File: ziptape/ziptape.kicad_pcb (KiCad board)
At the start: 2 copper layers, 62.5 x 34 mm, 13 parts, among them J1 Cassette_Playback, J2 Cassette_Record, J3 Conn_RIOT, J4 Conn_Adapter_A, J5 Conn_Adapter_B, U1 LM339

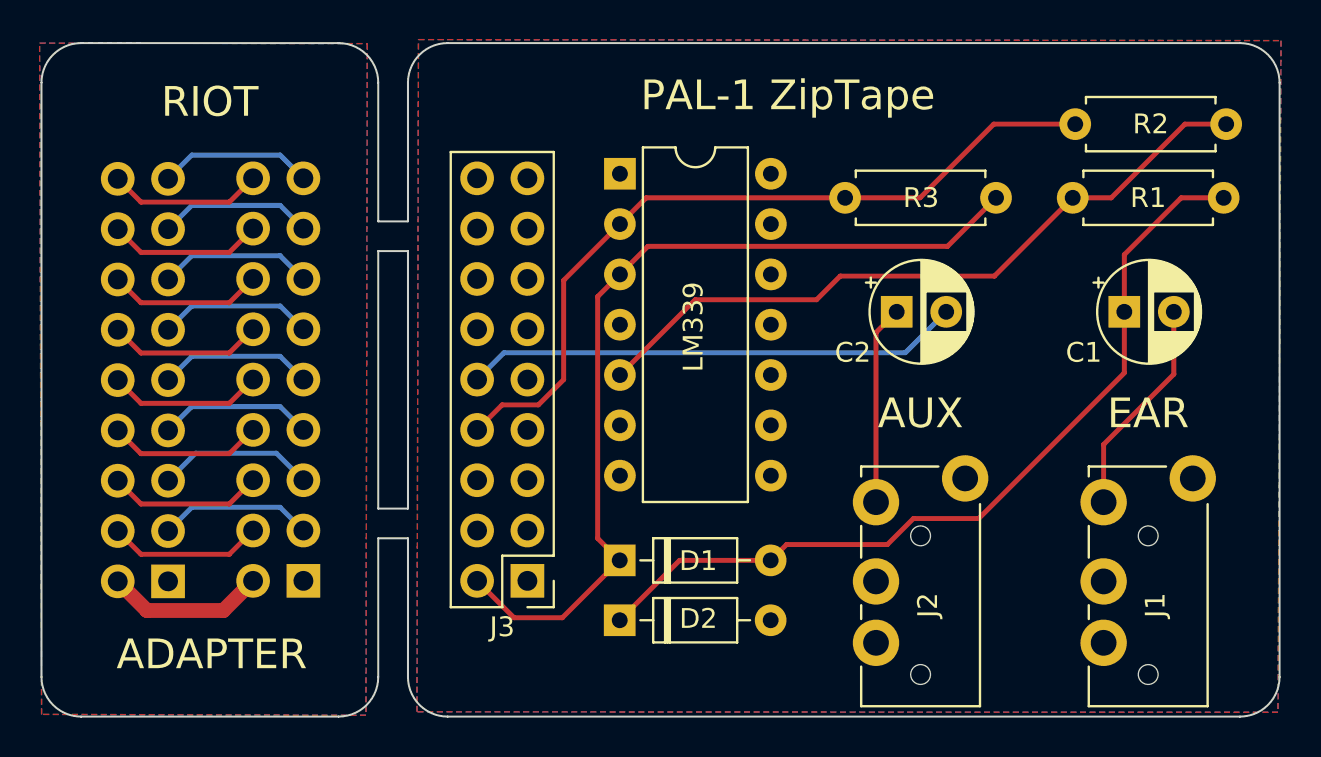
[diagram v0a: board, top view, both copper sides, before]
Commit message: Update audio sockets
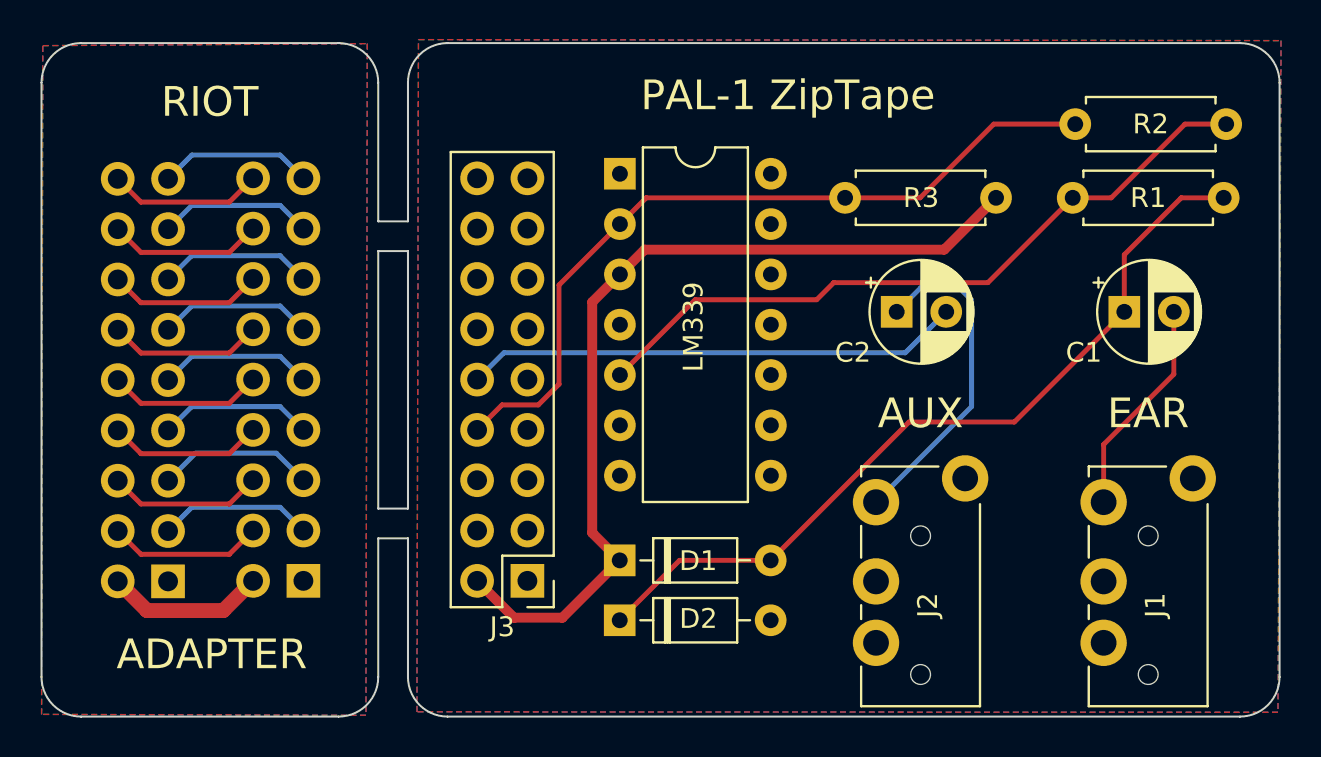
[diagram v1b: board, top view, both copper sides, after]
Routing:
- net Net-(C2-Pad1): track 10.0 -> 16.7 mm
- net Net-(C1-Pad1): track 42.8 -> 41.0 mm
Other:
- board text added: "2023"
- board text added: "Plastic Objects Limited"
